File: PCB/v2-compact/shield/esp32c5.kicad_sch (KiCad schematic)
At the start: 0 parts

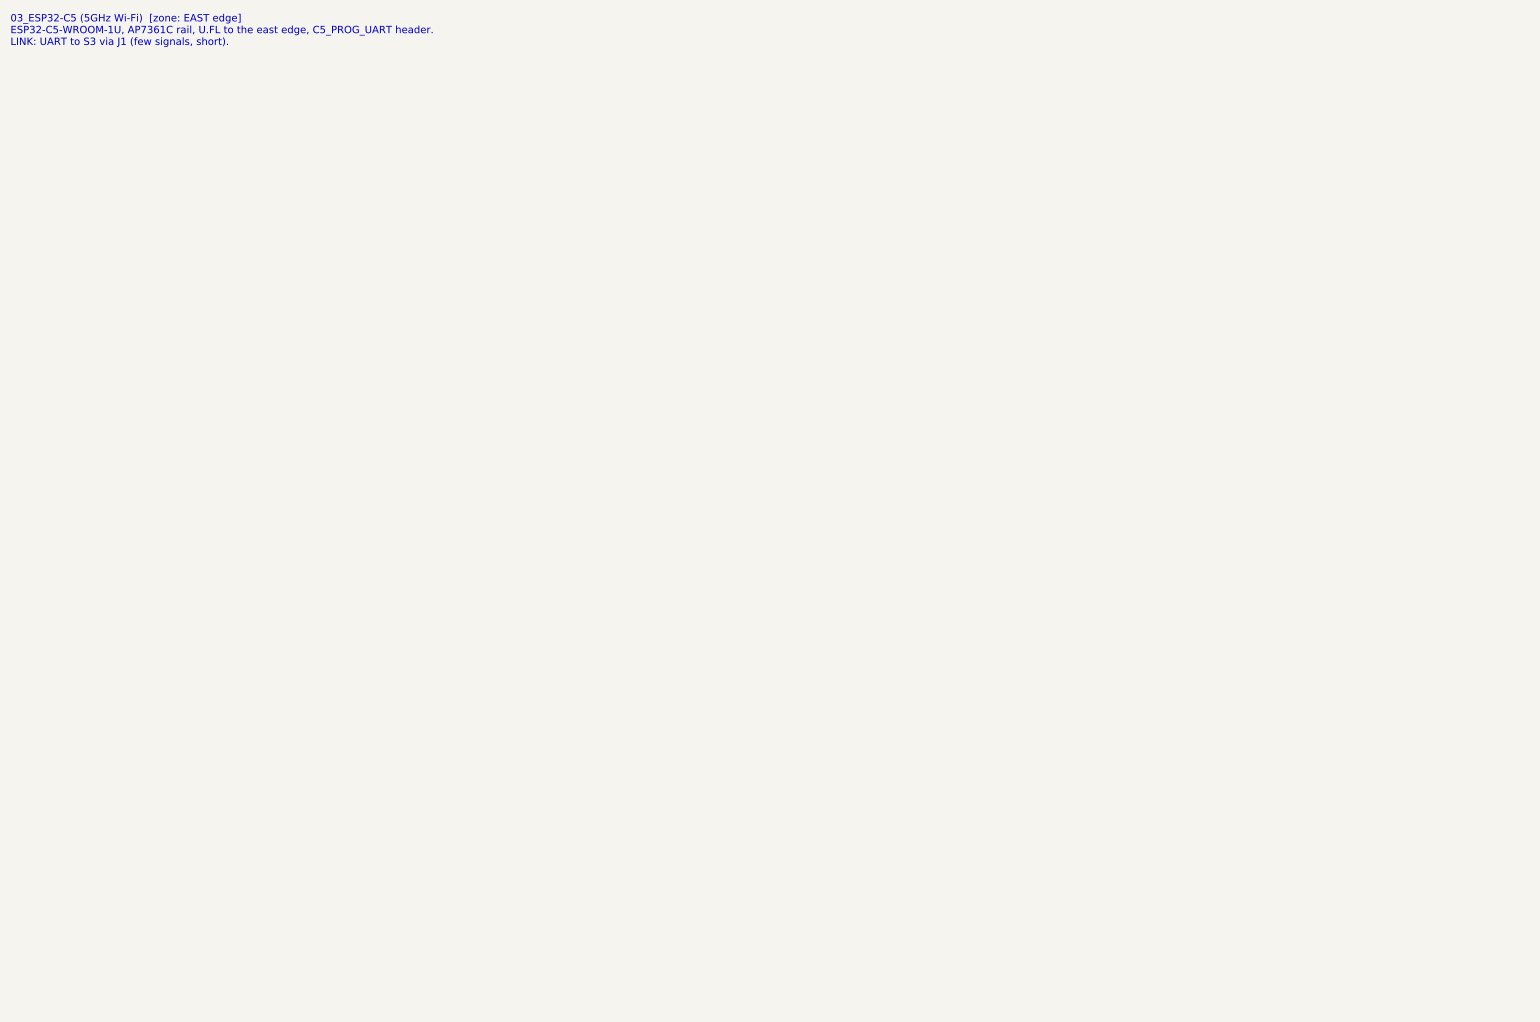
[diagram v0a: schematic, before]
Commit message: Schematics: ESP32-C5 hub sheet with MCP23S17 CS/IO expander
The C5's ~22 GPIO cannot drive all the radio control lines directly, so per the
plan the C5 sheet adds an MCP23S17 SPI I/O expander on the shield:
- C5 masters the SPI spine (SCK/MOSI/MISO), talks to the S3 over UART0 (also on
  the J40 prog header), and drives the timing-critical lines directly (the three
  nRF24 CE lines, SX1262 BUSY).
- MCP23S17 (U42) generates the seven chip-selects + SX1262 reset on its GPA
  outputs and reads the radio IRQs on its GPB inputs, all local to the shield.
- EN/boot RC + pull-ups, decoupling, U.FL on C5_ANT.

Netlist-verified: SPI_SCK/MISO reach every slave + master + expander; FLASH_CS
and the NRFn_CSN come from the expander outputs; C5_TX reaches J1 and the header.
Also renamed duplicate C55/C56 refs on the GPS sheet.
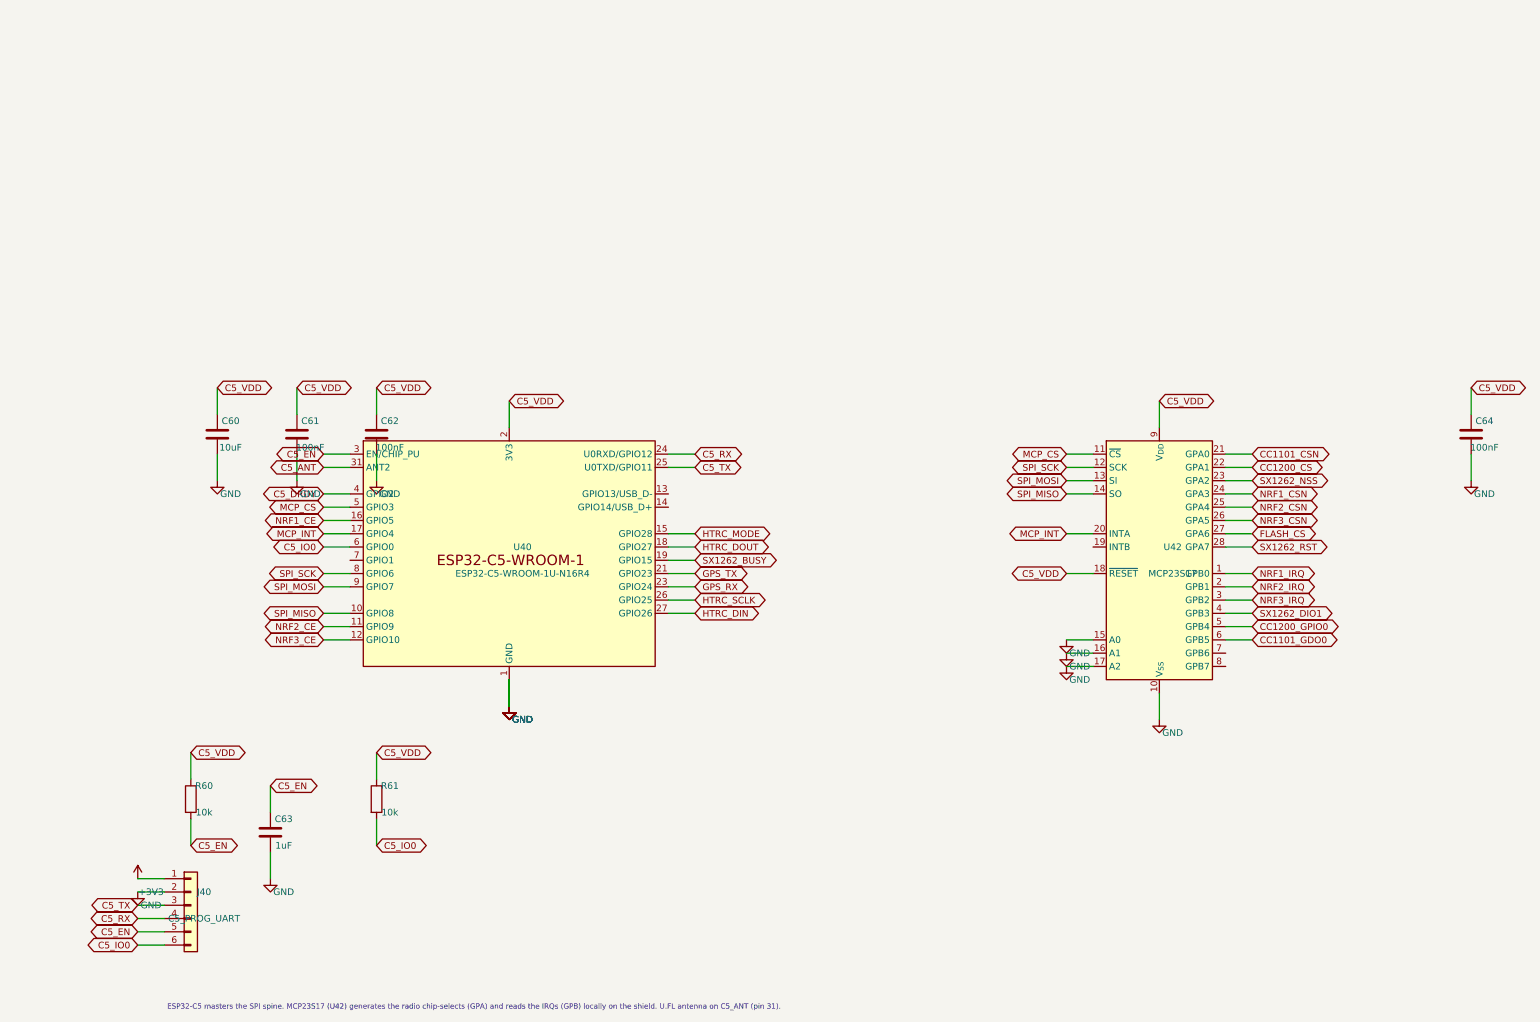
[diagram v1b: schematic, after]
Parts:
- added C60: 10uF, Capacitor_SMD:C_0402_1005Metric, symbol Device:C
- added C61, C62, C64: 100nF, Capacitor_SMD:C_0402_1005Metric, symbol Device:C
- added C63: 1uF, Capacitor_SMD:C_0402_1005Metric, symbol Device:C
- added J40: C5_PROG_UART, Connector_PinHeader_2.54mm:PinHeader_1x06_P2.54mm_Vertical, symbol Connector_Generic:Conn_01x06
- added R60, R61: 10k, Resistor_SMD:R_0402_1005Metric, symbol Device:R
- added U40: ESP32-C5-WROOM-1U-N16R4, symbol Espressif:ESP32-C5-WROOM-1U
- added U42: MCP23S17, Package_SO:SOIC-28W_7.5x17.9mm_P1.27mm, symbol Interface_Expansion:MCP23S17x-x-SO
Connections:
- new net +3V3: J40.1 (Pin_1)
- new net C5_ANT: U40.31 (ANT2)
- new net C5_DRDY: U40.4 (GPIO2)
- new net C5_EN: C63.1, J40.5 (Pin_5), R60.2, U40.3 (EN/CHIP_PU)
- new net C5_IO0: J40.6 (Pin_6), R61.2, U40.6 (GPIO0)
- new net C5_RX: J40.4 (Pin_4), U40.24 (U0RXD/GPIO12)
- new net C5_TX: J40.3 (Pin_3), U40.25 (U0TXD/GPIO11)
- new net C5_VDD: C60.1, C61.1, C62.1, C64.1, R60.1, R61.1, U40.2 (3V3), U42.18 (~{RESET}), U42.9 (V_{DD})
- new net CC1101_CSN: U42.21 (GPA0)
- new net CC1101_GDO0: U42.6 (GPB5)
- new net CC1200_CS: U42.22 (GPA1)
- new net CC1200_GPIO0: U42.5 (GPB4)
- new net FLASH_CS: U42.27 (GPA6)
- new net GND: C60.2, C61.2, C62.2, C63.2, C64.2, J40.2 (Pin_2), U40.1 (GND), U40.28 (GND), U40.29 (GND), U40.30 (GND), U40.32 (GND), U42.10 (V_{SS}), U42.15 (A0), U42.16 (A1), U42.17 (A2)
- new net GPS_RX: U40.23 (GPIO24)
- new net GPS_TX: U40.21 (GPIO23)
- new net HTRC_DIN: U40.27 (GPIO26)
- new net HTRC_DOUT: U40.18 (GPIO27)
- new net HTRC_MODE: U40.15 (GPIO28)
- new net HTRC_SCLK: U40.26 (GPIO25)
- new net MCP_CS: U40.5 (GPIO3), U42.11 (~{CS})
- new net MCP_INT: U40.17 (GPIO4), U42.20 (INTA)
- new net NRF1_CE: U40.16 (GPIO5)
- new net NRF1_CSN: U42.24 (GPA3)
- new net NRF1_IRQ: U42.1 (GPB0)
- new net NRF2_CE: U40.11 (GPIO9)
- new net NRF2_CSN: U42.25 (GPA4)
- new net NRF2_IRQ: U42.2 (GPB1)
- new net NRF3_CE: U40.12 (GPIO10)
- new net NRF3_CSN: U42.26 (GPA5)
- new net NRF3_IRQ: U42.3 (GPB2)
- new net SPI_MISO: U40.10 (GPIO8), U42.14 (SO)
- new net SPI_MOSI: U40.9 (GPIO7), U42.13 (SI)
- new net SPI_SCK: U40.8 (GPIO6), U42.12 (SCK)
- new net SX1262_BUSY: U40.19 (GPIO15)
- new net SX1262_DIO1: U42.4 (GPB3)
- new net SX1262_NSS: U42.23 (GPA2)
- new net SX1262_RST: U42.28 (GPA7)
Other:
- note added: "ESP32-C5 masters the SPI spine. MCP23S17 (U42) generates the radio chip-selects (GPA) and reads the IRQs (GPB) locally on the shield. U.FL antenna on C5_ANT (pin 31)."
- note removed: "03_ESP32-C5 (5GHz Wi-Fi) [zone: EAST edge] ESP32-C5-WROOM-1U, AP7361C rail, U.FL to the east edge, C5_PROG_UART header. LINK: UART to S3 via J1 (few signals, short)."

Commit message: PCB: import schematic netlists onto both boards (parts placed + nets assigned)
Load every footprint from the schematic into the floorplan-skeleton boards,
place each in its subsystem's zone (grid-spread, back-side sheets flipped), and
assign all nets. Shield: 79 parts, 419 pad-nets, 153 nets. Main: 29 parts,
150 pad-nets, 57 nets. Register the Espressif footprint library; add a
placeholder Core1106 SoM footprint; assign the C5 (Espressif), NEO-M9N (ublox_NEO)
and CC1101 (2x4 header) module footprints.

This is the initial import: every part is on its board with the full ratsnest,
ready for placement refinement and routing.
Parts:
- U40: footprint (none) -> Espressif:ESP32-C5-WROOM-1U
